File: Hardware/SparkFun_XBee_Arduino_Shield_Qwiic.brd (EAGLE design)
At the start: 53.3 x 59.7 mm, 158 parts, among them J4 QWIIC_RIGHT_ANGLE, U1 FSUSB30MUX_MSOP10, U2 AP63203, U3 ESD Diode, U4 FT231XS, U5 ESD Diode, U6 TXS0108, U7 TXS0108

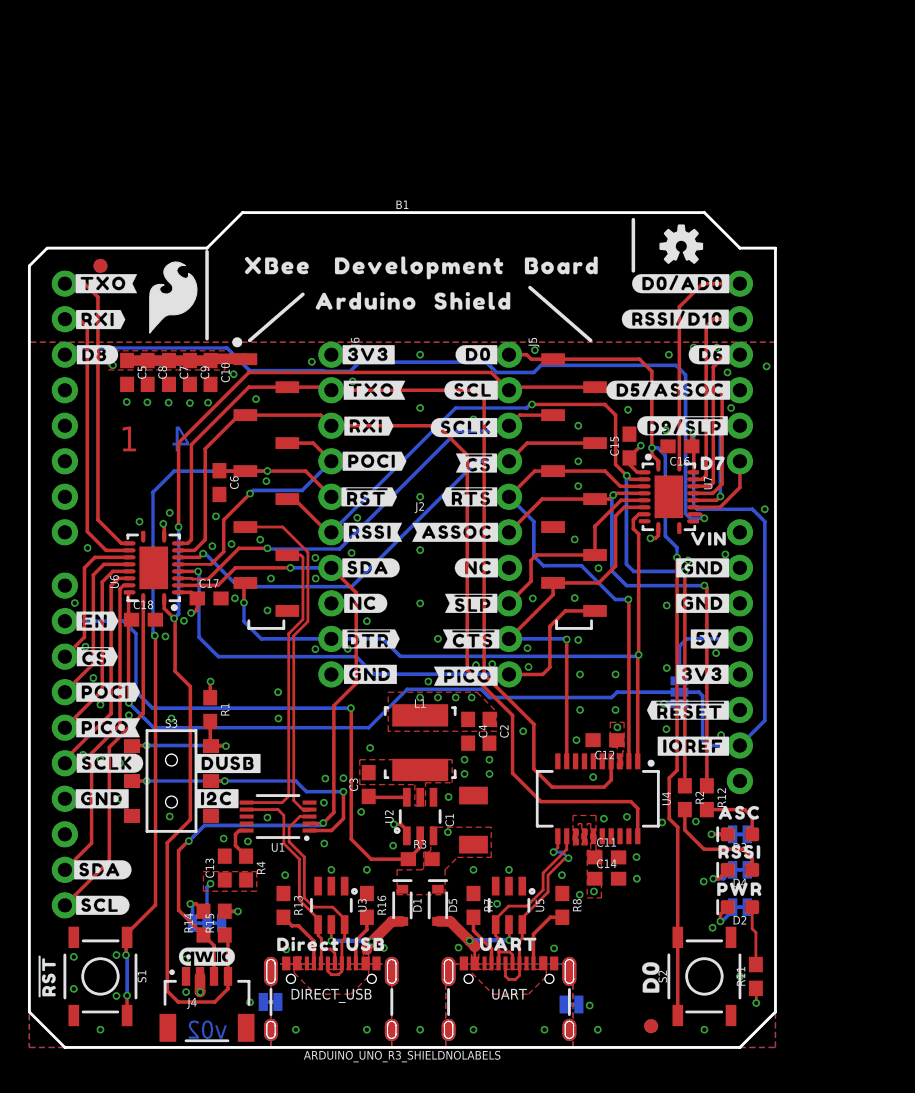
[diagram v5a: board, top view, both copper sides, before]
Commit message: Adds new power control circuits
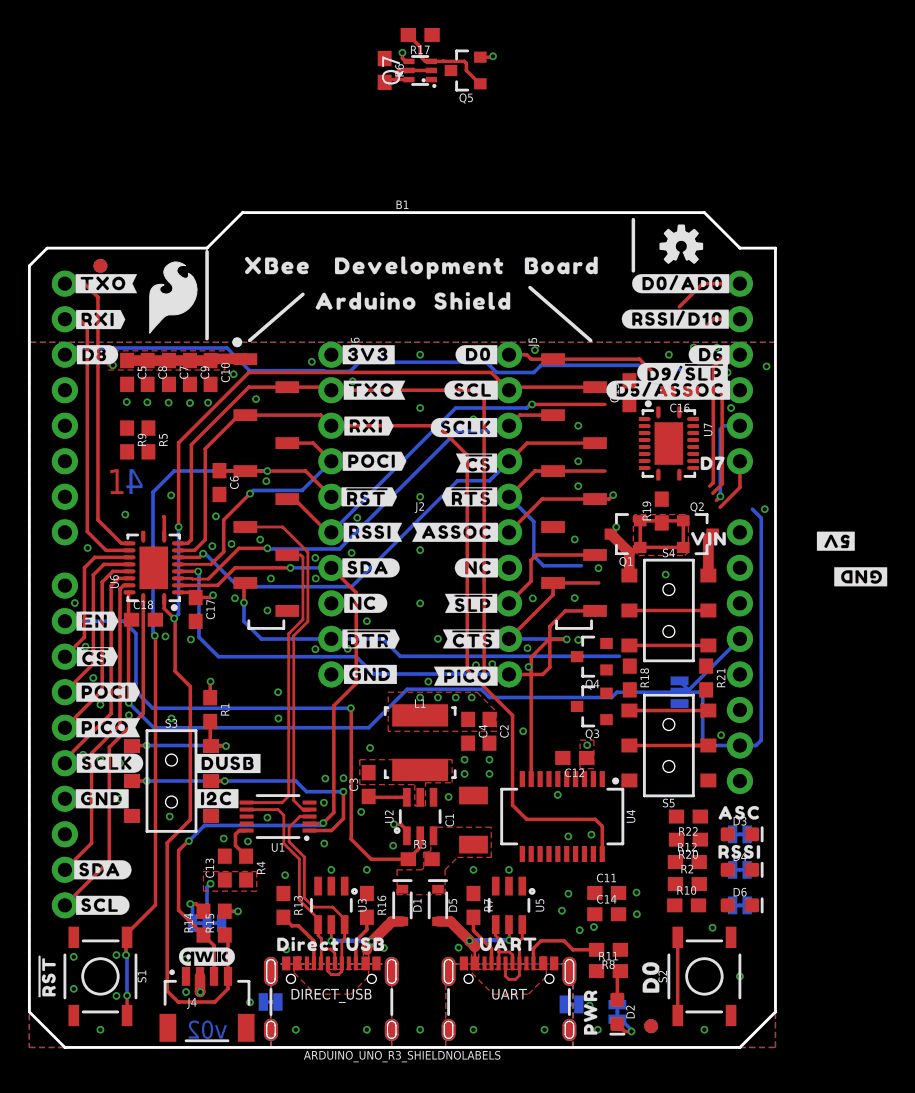
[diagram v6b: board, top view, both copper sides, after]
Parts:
- removed U$12: (no value), topmirror:#GND#0
- removed U$44: (no value), top:#3V3#1
- removed U$87: (no value), top:##RESET##23
- removed U$88: (no value), top:#IOREF#6
- added D6: GREEN, SparkFun-LED:LED-0603
- added IO4: JUMPER-SMT_2_NC_TRACE_SILK, SparkFun-Jumpers:SMT-JUMPER_2_NC_TRACE_SILK
- added Q1, Q2, Q3: 3.1A/30V/105mΩ, SparkFun-DiscreteSemi:SOT23-3
- added Q4: 5.8A/30V/35mΩ, SparkFun-DiscreteSemi:SOT23-3
- added Q5: 20V/4.2A/52mΩ/1.4W, SparkFun-DiscreteSemi:SOT23-3
- added Q7: (no value), SparkFun-DiscreteSemi:SOT363_PHILIPS
- added R10: 330, SparkFun-Resistors:0603
- added R17: 1M, SparkFun-Resistors:0603
- added R18, R19, R20, R21, R22, R5, R9: 10k, SparkFun-Resistors:0603
- added R6: 100k, SparkFun-Resistors:0603
- added S4, S5: (no value), SparkFun-Switches:SWITCH_DPDT_SMD_AYZ0202
- moved U$2 13.8 mm to (40.1, 2.54), turned to 90 degrees
- moved D2 11.5 mm to (42.0, 2.54), turned to 270 degrees
- moved PLED 11.5 mm to (42.0, 2.54), turned to 270 degrees
- moved U$39 11.4 mm to (57.7, 36.2), turned to 180 degrees
- moved U$29 11.3 mm to (59.4, 33.7), turned to 180 degrees
- moved R11 10.5 mm to (41.4, 5.46), turned to 0 degrees
- moved U$42 9.02 mm to (44.6, 37.1), turned to 270 degrees
- moved U$52 6.35 mm to (45.5, 3.94), turned to 180 degrees
- moved R2 6.17 mm to (47.0, 11.7), turned to 0 degrees
- moved R12 4.80 mm to (47.0, 13.3), turned to 0 degrees
- moved R8 4.58 mm to (41.4, 6.99), turned to 180 degrees
- moved C16 3.81 mm to (46.5, 46.8)
- moved U7 3.81 mm to (45.7, 43.2)
- moved C15 3.81 mm to (42.9, 46.8)
- moved U$8 3.81 mm to (46.9, 48.3)
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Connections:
- new net 3.3V_SW: B1.3.3V
- new net 3.3V_VREG: C2.1, C4.1, L1.P$2, Q5.3, Q7.1, U2.1
- new net 3V3_R3: Q3.2, S5.3, S5.6
- new net N$16: R20.2, S5.1, S5.4
- new net N$17: D6.C, IO4.2
- new net N$18: Q4.3, R19.2
- new net N$19: Q7.2, Q7.5, Q7.6, R6.2
- new net N$20: Q5.1, Q7.3, R17.2
- new net N$22: Q4.1, R21.1
- new net N$24: R18.2, S4.3, S4.6
- new net N$25: Q1.1, Q1.2, Q2.1, Q2.2, R19.1
- new net N$26: R22.2, S5.2, S5.5
- new net N$27: Q3.1, R22.1
- new net N$4: D6.A, R10.2
- new net N$9: R21.2, S4.2, S4.5
- new net OE_BUS: B1.D3, R5.2, U6.10
- new net OE_IO: B1.D4, R9.2, U7.10
- new net VIN_R3: B1.VIN, Q2.3, S4.1
- net 3.3V: now also Q3.3, Q5.2, Q7.4; no longer B1.3.3V, C2.1, C4.1, L1.P$2, U2.1, U6.10, U7.10
- net D4/SPI_PICO: now also R10.1
- net GND: now also IO4.1, Q4.2, R17.1, R18.1, R20.1, R5.1, R6.1, R9.1
- net VIN: now also Q1.3, S4.4; no longer B1.VIN
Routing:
- net D0: track 59.6 -> 16.3 mm, vias 2 -> 0
- net VIN: track 40.8 -> 3.51 mm, vias 1 -> 0
- net D10/RSSI_PWM: track 60.6 -> 27.5 mm, vias 3 -> 1
- net D5/ASSOCIATE: track 37.7 -> 8.70 mm, vias 2 -> 1
- net D8/!DTR!: track 50.4 -> 30.7 mm, vias 2 -> 1
- net D6/!RTS!: track 35.4 -> 16.3 mm, vias 1 -> 0
- net 3.3V: track 35.1 -> 18.4 mm, vias 18 -> 13
- net D13/TXO: track 66.3 -> 50.5 mm
- net D8/!DTR!-TRANS: track 58.6 -> 46.3 mm, vias 1 -> 0
- net IOREF: track 88.0 -> 76.1 mm, vias 2 -> 1
- net D10/RSSI_PWM-TRANS: track 14.3 -> 2.62 mm
- net 3.3V_VREG: track 0.00 -> 11.3 mm, vias 0 -> 2
- net D0-TRANS: track 16.3 -> 5.02 mm
- net N$25: track 0.00 -> 10.1 mm
- net D-: track 13.7 -> 4.55 mm
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- added copper zone on layer 1, net N$25

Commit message: Routes most of the new air wires
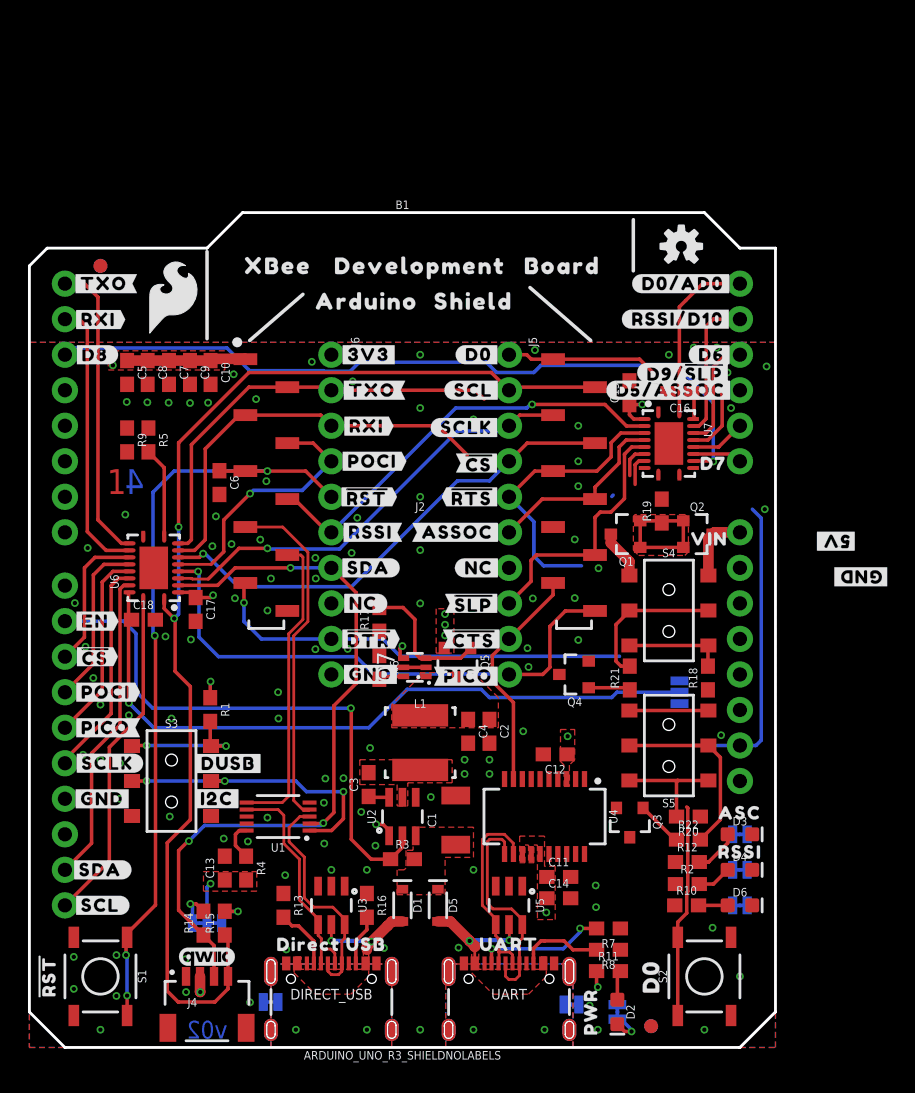
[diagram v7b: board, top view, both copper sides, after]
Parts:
- moved Q7 42.7 mm to (27.6, 27.2)
- moved R6 42.7 mm to (25.0, 27.2)
- moved Q5 42.3 mm to (30.6, 27.6), turned to 180 degrees
- moved R17 41.9 mm to (25.0, 30.6), turned to 90 degrees
- moved U$89 16.5 mm to (64.8, 25.4)
- moved U$67 12.0 mm to (58.4, 21.1)
- moved R7 9.79 mm to (41.4, 8.51), turned to 180 degrees
- moved Q3 8.68 mm to (42.9, 16.1), turned to 180 degrees
- moved R18 5.59 mm to (48.5, 26.4), turned to 90 degrees
- moved R21 5.46 mm to (42.9, 26.4), turned to 90 degrees
- moved C11 3.61 mm to (37.8, 12.2)
- moved C14 3.61 mm to (37.8, 10.7)
- moved Q4 1.80 mm to (39.0, 26.7)
- moved R20 1.65 mm to (47.1, 16.5)
- moved R22 1.65 mm to (47.1, 14.9), turned to 0 degrees
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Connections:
- removed net 3.3V_SW: B1.3.3V
- net 3V3_R3: now also B1.3.3V
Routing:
- net D14/RXI: track 65.0 -> 29.6 mm
- net D13/TXO: track 50.5 -> 30.8 mm
- net D9/!SLEEP!: track 8.46 -> 18.6 mm
- net D+: track 6.32 -> 16.3 mm, vias 1 -> 0
- net D-: track 4.55 -> 14.4 mm
- net D0: track 16.3 -> 25.9 mm
- net D8/!DTR!-TRANS: track 46.3 -> 54.7 mm, vias 0 -> 1
- net N$16: track 0.00 -> 8.27 mm
- net D10/RSSI_PWM-TRANS: track 2.62 -> 10.3 mm
- net N$26: track 6.79 -> 14.5 mm
- net D0-TRANS: track 5.02 -> 12.5 mm
- net 5V: track 6.11 -> 0.00 mm
- net D7/!CTS!: track 24.5 -> 18.7 mm, vias 1 -> 0
- net N$6: track 3.83 -> 9.32 mm, vias 0 -> 2
- net N$9: track 5.65 -> 10.8 mm
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- added copper zone on layer 1, net 3.3V_VREG

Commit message: Improvements to power selection
* Routes airwires
* Fixes some silk
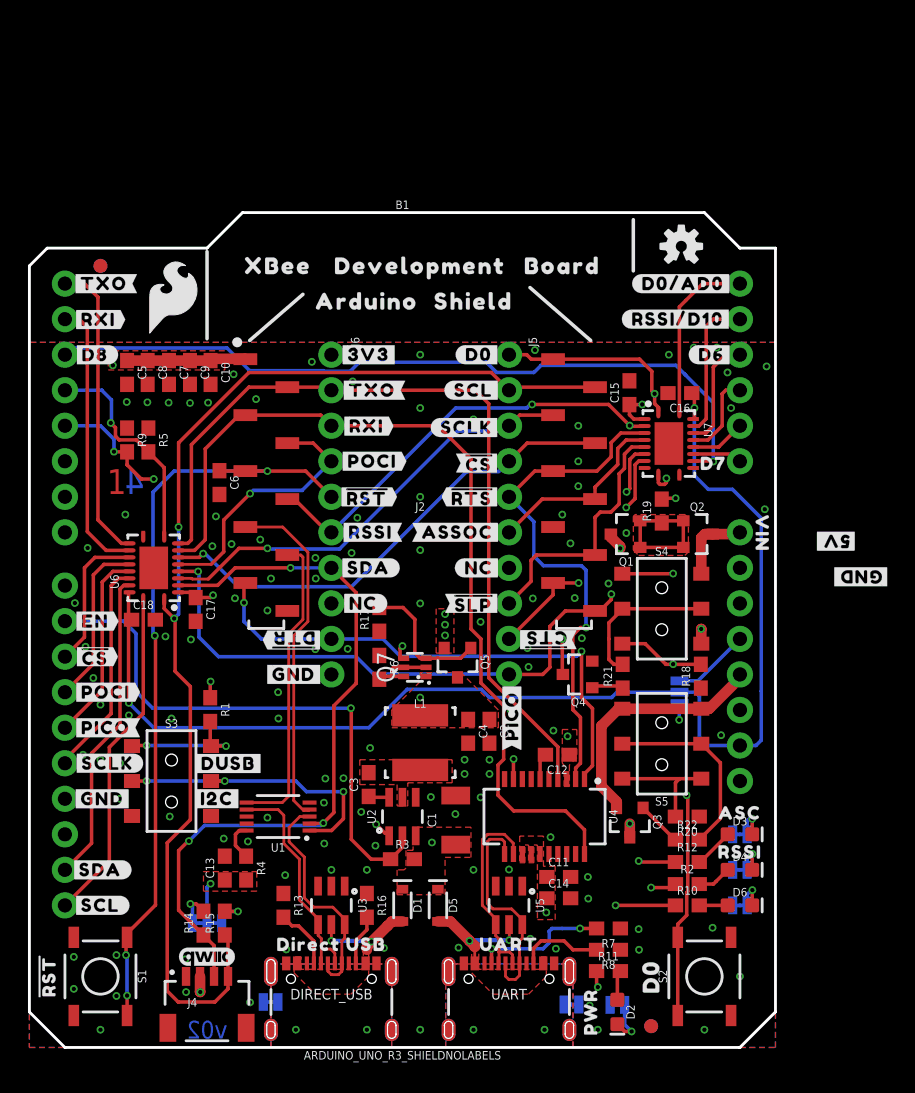
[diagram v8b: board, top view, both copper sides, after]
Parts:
- removed U$41: (no value), topmirror:#D5#ASSOC#25
- removed U$8: (no value), topmirror:#D9##SLP##28
- R18: value 10k -> 100k
- moved U$89 20.0 mm to (44.8, 26.6), turned to 270 degrees
- moved U$50 5.49 mm to (18.9, 26.7)
- moved U$69 5.36 mm to (18.9, 29.1), turned to 180 degrees
- moved U$31 5.18 mm to (36.9, 29.2), turned to 180 degrees
- moved U$70 4.23 mm to (34.5, 23.7), turned to 90 degrees
- moved U$66 3.80 mm to (52.4, 36.8), turned to 270 degrees
- moved U$52 0.91 mm to (45.5, 3.02)
- moved R18 0.52 mm to (48.0, 26.5)
- moved R21 0.52 mm to (42.4, 26.5)
- moved S4 0.52 mm to (45.2, 31.4)
- moved S5 0.52 mm to (45.2, 21.7)
- moved PLED 0.51 mm to (42.0, 3.05), turned to 180 degrees
- moved Q4 0.25 mm to (39.2, 26.7)
- moved C12 0.15 mm to (37.7, 20.9)
- moved R20 0.08 mm to (47.0, 16.5)
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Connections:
- net N$24: now also S4.4; no longer S4.3
- net VIN: now also S4.3; no longer S4.4
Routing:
- net OE_IO: track 0.00 -> 47.2 mm, vias 0 -> 3
- net VIN: track 3.51 -> 40.0 mm, vias 0 -> 3
- net D10/RSSI_PWM: track 30.9 -> 67.1 mm, vias 1 -> 3
- net D5/ASSOCIATE: track 13.7 -> 48.6 mm, vias 0 -> 2
- net D0: track 25.9 -> 60.5 mm, vias 0 -> 2
- net D14/RXI: track 29.6 -> 64.1 mm
- net D13/TXO: track 30.8 -> 60.1 mm
- net D4/SPI_PICO: track 39.1 -> 67.7 mm, vias 1 -> 3
- net D8/!DTR!: track 32.8 -> 54.1 mm, vias 1 -> 3
- net N$18: track 0.00 -> 21.1 mm, vias 0 -> 3
- net D6/!RTS!: track 20.8 -> 37.2 mm, vias 0 -> 1
- net IOREF: track 73.0 -> 87.8 mm, vias 1 -> 2
- net D7/!CTS!: track 18.7 -> 33.1 mm, vias 0 -> 3
- net 3V3_R3: track 5.65 -> 17.9 mm
- net N$24: track 7.14 -> 16.4 mm, vias 0 -> 2
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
